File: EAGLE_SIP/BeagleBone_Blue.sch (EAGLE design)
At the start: 200 parts, among them IC1 WL1835MODGBMOCT, J1 USD_CONNECTOR, M1 JST_ZH_2, M2 JST_ZH_2, M3 JST_ZH_2, M4 JST_ZH_2, Q3 MOSFET-N, U1 LOGIC-TXS0102DCTR(MSOP8), U5 24LC_32AT-I/OT, U6 SN74LVC1G07_DCK_5, Y1 CM200C-32.768KAZF-UT, Y2 445C33D24M00000

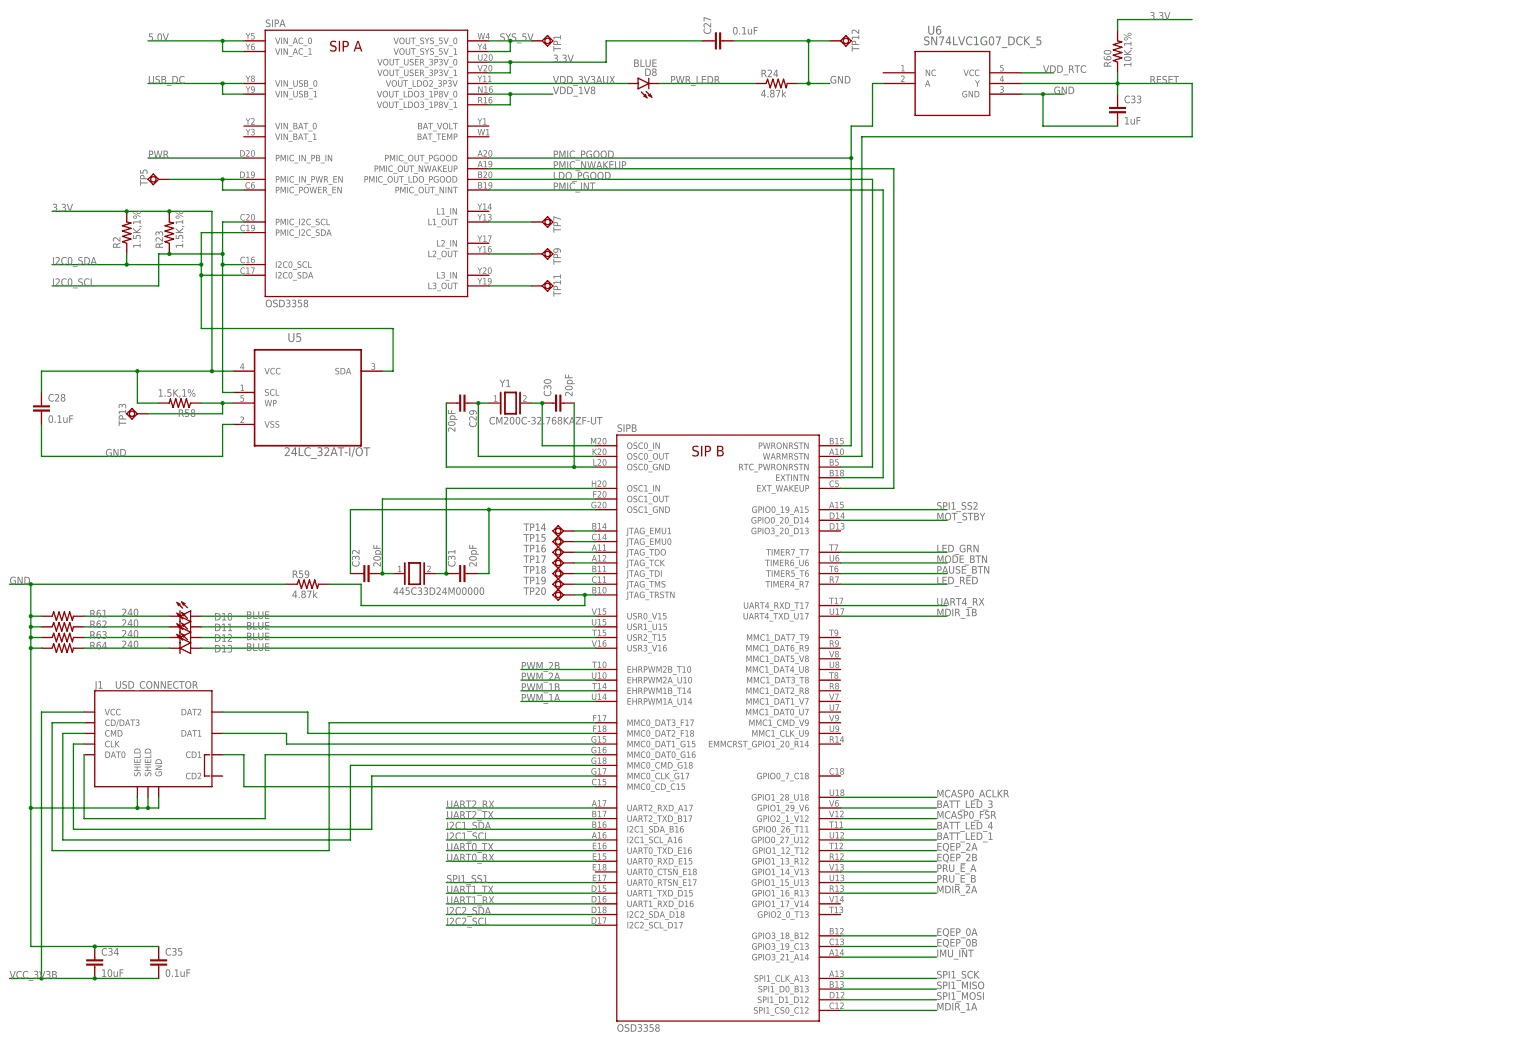
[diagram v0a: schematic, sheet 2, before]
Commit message: Revert "Remove eMMC for now since will not route at 5 mil"
This reverts commit 75f1e67d3ee9893e94103e41b84841ae77a6b699.

Conflicts:
	EAGLE_SIP/BeagleBone_Blue.brd
	EAGLE_SIP/BeagleBone_Blue.sch
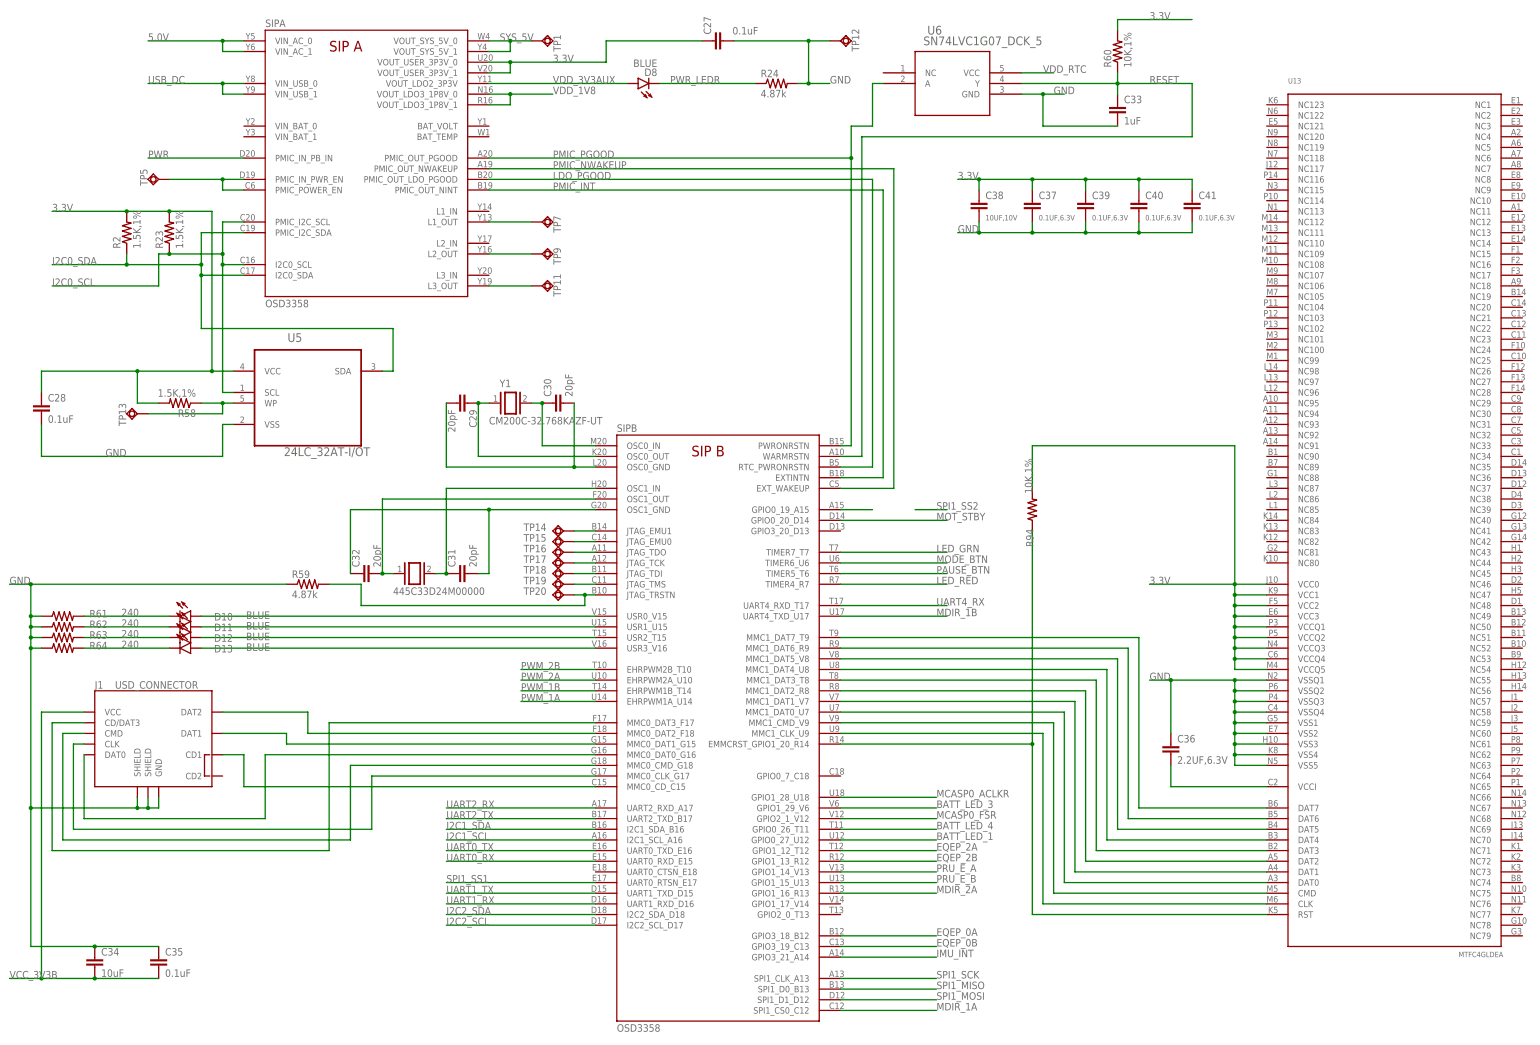
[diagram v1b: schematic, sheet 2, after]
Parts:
- added C36: 2.2UF,6.3V, Strawson_Eagle_Lib:CAP0402-CAP
- added C37, C39, C40, C41: 0.1UF,6.3V, Strawson_Eagle_Lib:CAP0402-CAP
- added C38: 10UF,10V, Strawson_Eagle_Lib:CAP0805
- added R94: 10K,1%, Strawson_Eagle_Lib:RESISTOR0402-RES
- added U8: MTFC4GLDEA, BeagleBone_Blue:MTFC4GLDEA
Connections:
- new net N$109: C36.2, U8.VCCI
- new net N$86: SIPB.GPIO0_19_A15
- new net N$88: SIPB.MMC1_DAT7_T9, U8.DAT7
- new net N$89: SIPB.MMC1_DAT6_R9, U8.DAT6
- new net N$90: SIPB.MMC1_DAT5_V8, U8.DAT5
- new net N$91: SIPB.MMC1_DAT4_U8, U8.DAT4
- new net N$92: SIPB.MMC1_DAT3_T8, U8.DAT3
- new net N$93: SIPB.MMC1_DAT2_R8, U8.DAT2
- new net N$94: SIPB.MMC1_DAT1_V7, U8.DAT1
- new net N$95: SIPB.MMC1_DAT0_U7, U8.DAT0
- new net N$96: SIPB.MMC1_CMD_V9, U8.CMD
- new net N$97: SIPB.MMC1_CLK_U9, U8.CLK
- new net N$98: R94.1, SIPB.EMMCRST_GPIO1_20_R14, U8.RST
- net 3.3V: now also C37.1, C38.1, C39.1, C40.1, C41.1, R94.2, U8.VCC0, U8.VCC1, U8.VCC2, U8.VCC3, U8.VCCQ1, U8.VCCQ2, U8.VCCQ3, U8.VCCQ4, U8.VCCQ5
- net GND: now also C36.1, C37.2, C38.2, C39.2, C40.2, C41.2, U8.VSS1, U8.VSS2, U8.VSS3, U8.VSS4, U8.VSS5, U8.VSSQ1, U8.VSSQ2, U8.VSSQ3, U8.VSSQ4
- net SPI1_SS2: no longer SIPB.GPIO0_19_A15

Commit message: SPI1_SS2: net connect
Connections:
- removed net N$86: SIPB.GPIO0_19_A15
- net SPI1_SS2: now also SIPB.GPIO0_19_A15
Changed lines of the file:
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@@
-</segment>
-</net>
-<net name="N$86" class="0">
-<segment>
-<pinref part="SIP" gate="B" pin="GPIO0_19_A15"/>
-<wire x1="208.28" y1="132.08" x2="215.9" y2="132.08" width="0.1524" layer="91"/>
 </segment>
 </net>
 <net name="SPI1_SS2" class="0">
 <segment>
-<wire x1="226.06" y1="132.08" x2="233.68" y2="132.08" width="0.1524" layer="91"/>
 <label x="231.14" y="132.08" size="1.778" layer="95"/>
+<pinref part="SIP" gate="B" pin="GPIO0_19_A15"/>
+<wire x1="233.68" y1="132.08" x2="208.28" y2="132.08" width="0.1524" layer="91"/>
 </segment>
 </net>
@@
 </segment>
 </net>
-=======
 <net name="N$88" class="0">
 <segment>

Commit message: Add resistor to MMC1_CLK
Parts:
- added R15: 33, Strawson_Eagle_Lib:RESISTOR0402-RES
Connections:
- new net N$85: R15.1, SIPB.MMC1_CLK_U9
- net N$97: now also R15.2; no longer SIPB.MMC1_CLK_U9
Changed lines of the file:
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@@
 <part name="R9" library="Strawson_Eagle_Lib" deviceset="RESISTOR" device="0402-RES" value="4.87k"/>
 <part name="GND10" library="supply1" deviceset="GND" device=""/>
+<part name="R15" library="Strawson_Eagle_Lib" deviceset="RESISTOR" device="0402-RES" value="33"/>
 </parts>
 <sheets>
@@
 <instance part="U6" gate="A" x="218.44" y="236.22"/>
 <instance part="J1" gate="1" x="43.18" y="78.74"/>
+<instance part="R15" gate="G$1" x="218.44" y="78.74" smashed="yes">
+<attribute name="NAME" x="224.79" y="80.2386" size="1.778" layer="95" align="top-left"/>
+<attribute name="VALUE" x="232.41" y="80.518" size="1.778" layer="96" align="top-left"/>
+</instance>
 </instances>
 <busses>
@@
 <net name="N$97" class="0">
 <segment>
-<pinref part="SIP" gate="B" pin="MMC1_CLK_U9"/>
-<wire x1="208.28" y1="78.74" x2="256.54" y2="78.74" width="0.1524" layer="91"/>
 <wire x1="256.54" y1="78.74" x2="256.54" y2="38.1" width="0.1524" layer="91"/>
 <pinref part="U8" gate="G$1" pin="CLK"/>
 <wire x1="256.54" y1="38.1" x2="309.88" y2="38.1" width="0.1524" layer="91"/>
+<pinref part="R15" gate="G$1" pin="2"/>
+<wire x1="223.52" y1="78.74" x2="256.54" y2="78.74" width="0.1524" layer="91"/>
 </segment>
 </net>
@@
 </segment>
 </net>
+<net name="N$85" class="0">
+<segment>
+<pinref part="SIP" gate="B" pin="MMC1_CLK_U9"/>
+<pinref part="R15" gate="G$1" pin="1"/>
+<wire x1="208.28" y1="78.74" x2="213.36" y2="78.74" width="0.1524" layer="91"/>
+</segment>
+</net>

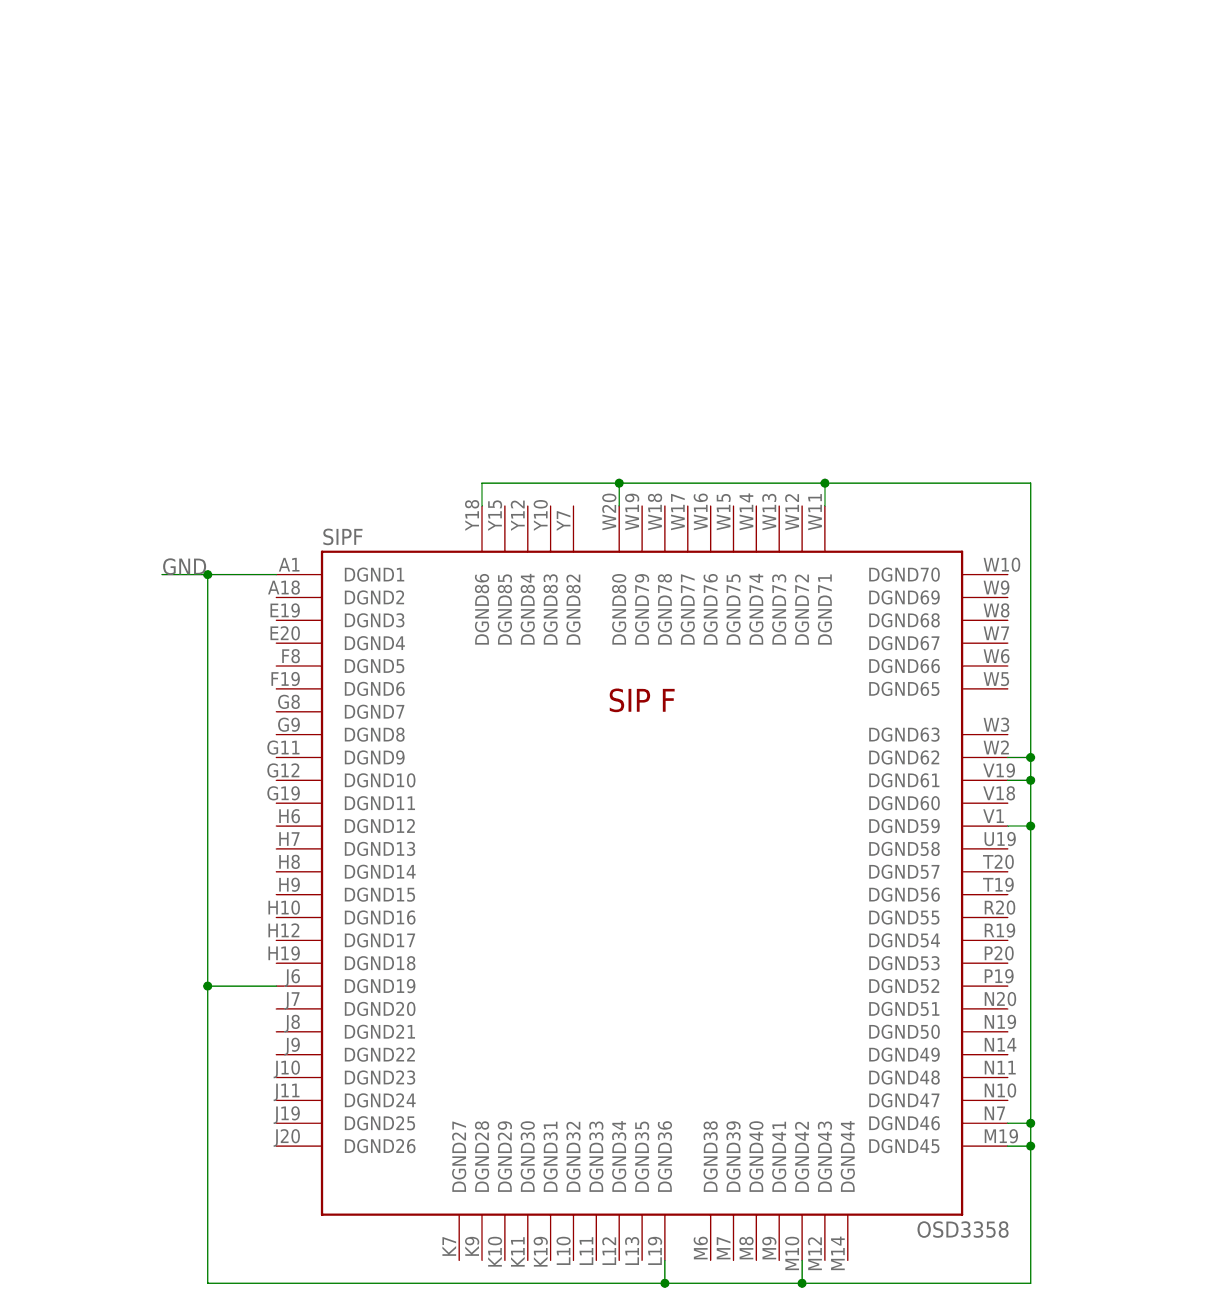
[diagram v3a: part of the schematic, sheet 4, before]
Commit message: Connected GND for SiP
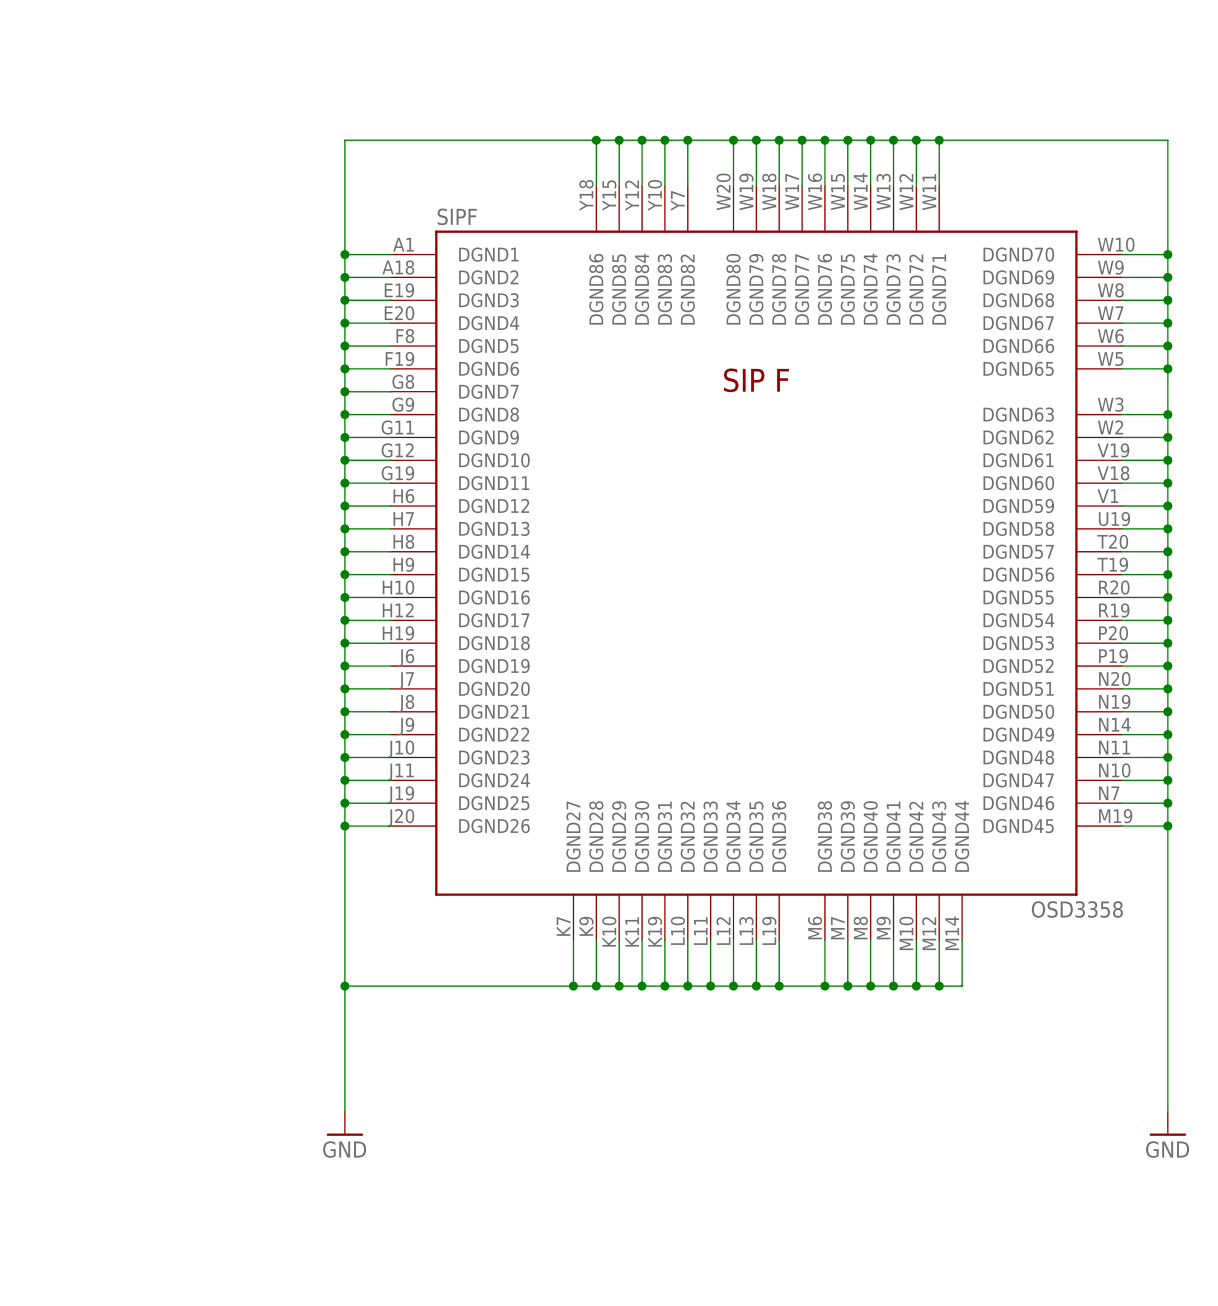
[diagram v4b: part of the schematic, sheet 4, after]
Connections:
- net GND: now also SIPF.DGND10, SIPF.DGND11, SIPF.DGND12, SIPF.DGND13, SIPF.DGND14, SIPF.DGND15, SIPF.DGND16, SIPF.DGND17, SIPF.DGND18, SIPF.DGND2, SIPF.DGND20, SIPF.DGND21, SIPF.DGND22, SIPF.DGND23, SIPF.DGND24, SIPF.DGND25, SIPF.DGND26, SIPF.DGND27, SIPF.DGND28, SIPF.DGND29, SIPF.DGND3, SIPF.DGND30, SIPF.DGND31, SIPF.DGND32, SIPF.DGND33, SIPF.DGND34, SIPF.DGND35, SIPF.DGND38, SIPF.DGND39, SIPF.DGND4, SIPF.DGND40, SIPF.DGND41, SIPF.DGND43, SIPF.DGND44, SIPF.DGND47, SIPF.DGND48, SIPF.DGND49, SIPF.DGND5, SIPF.DGND50, SIPF.DGND51, SIPF.DGND52, SIPF.DGND53, SIPF.DGND54, SIPF.DGND55, SIPF.DGND56, SIPF.DGND57, SIPF.DGND58, SIPF.DGND6, SIPF.DGND60, SIPF.DGND63, SIPF.DGND65, SIPF.DGND66, SIPF.DGND67, SIPF.DGND68, SIPF.DGND69, SIPF.DGND7, SIPF.DGND70, SIPF.DGND72, SIPF.DGND73, SIPF.DGND74, SIPF.DGND75, SIPF.DGND76, SIPF.DGND77, SIPF.DGND78, SIPF.DGND79, SIPF.DGND8, SIPF.DGND82, SIPF.DGND83, SIPF.DGND84, SIPF.DGND85, SIPF.DGND9
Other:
- moved on the sheet: SIPF, UART0
